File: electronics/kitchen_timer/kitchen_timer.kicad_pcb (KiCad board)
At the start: 2 copper layers, 76.5 x 84.5 mm, 30 parts, among them J1 JST_2pin_2.5mm, J2 UART, J3 SWD, Q1 BC327, Q2 BC327, Q3 BC327, Q4 BC327, Q5 BC337, SW1 BTN_A, SW2 BTN_B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

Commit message: Add 3d models to components, small rerouting
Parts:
- added H1: M2 hole, MountingHole:MountingHole_2.2mm_M2_Pad_Via, F.Cu at (74.0, 91.8)
- added H2: M2 hole, MountingHole:MountingHole_2.2mm_M2_Pad_Via, F.Cu at (139.0, 91.8)
- added H3: M2 hole, MountingHole:MountingHole_2.2mm_M2_Pad_Via, F.Cu at (139.0, 20.8)
- added H4: M2 hole, MountingHole:MountingHole_2.2mm_M2_Pad_Via, F.Cu at (74.0, 20.8)
- J1: moved to B.Cu
- moved J1 39.6 mm to (122.2, 55.5), turned to 0 degrees
- moved J2 9.91 mm to (124.2, 92.0), turned to -90 degrees
- moved SW1 4.15 mm to (134.8, 31.5)
- moved SW2 4.15 mm to (134.8, 51.5)
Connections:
- U2 pad 23: unconnected-(U2-GND-Pad23) -> GND
- U2 pad 28: unconnected-(U2-GND-Pad28) -> GND
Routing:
- net Net-(U2-GPIO4): track 112.4 -> 79.7 mm
- net /charging_and_audio/VSYS: track 29.2 -> 18.8 mm
- net Net-(U2-GPIO8): track 63.7 -> 55.7 mm
- net Net-(J2-Pin_2): track 10.8 -> 4.16 mm
- net Net-(U2-GPIO10): track 81.9 -> 75.9 mm
- net Net-(U2-GPIO12): track 68.8 -> 62.8 mm
- net Net-(U2-GPIO14): track 89.4 -> 85.4 mm
- net Net-(U2-GPIO5): track 71.1 -> 67.3 mm
- net Net-(U2-GPIO11): track 75.8 -> 73.3 mm
- net Net-(Q1-B): track 6.19 -> 7.92 mm
- net Net-(J2-Pin_3): track 5.33 -> 4.16 mm
- net Net-(U2-GPIO13): track 68.2 -> 67.0 mm
- net Net-(U2-GPIO15): track 73.6 -> 72.5 mm
- net /charging_and_audio/PWM_SPEAKER: track 14.0 -> 13.0 mm
- net IN_2: track 31.9 -> 31.3 mm
- added copper zone on B.Cu, net GND
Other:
- board size 76.5 x 84.5 mm -> 74.2 x 79 mm

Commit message: Update electronics
- added Schottky diode and solder bridge
- corrected all errors from design rules checker
- added silk screen logos
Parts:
- added D1: SEMTECH BAT54S, Package_TO_SOT_SMD:TSOT-23, B.Cu at (119.0, 56.2)
- added G***: LOGO, LOGO, F.Cu at (104.2, 78.8)
- added G***: LOGO, LOGO, F.Cu at (127.8, 23.8)
- added JP1: SCHOTTKY_JUMPER, Jumper:SolderJumper-2_P1.3mm_Open_Pad1.0x1.5mm, B.Cu at (118.8, 51.5)
- added TP1: PWM_SPEAKER, TestPoint:TestPoint_Pad_2.0x2.0mm, F.Cu at (105.5, 66.8)
- U2: value Pico -> Raspberry Pi Pico
- moved J1 3.50 mm to (125.8, 55.5), turned to 90 degrees
- moved R14 1.77 mm to (132.2, 58.8)
- moved Q5 1.03 mm to (127.2, 62.8)
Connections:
- net /charging_and_audio/PWM_SPEAKER renamed /PWM_SPEAKER
- J1 pad 1: /charging_and_audio/VSYS -> /charging_and_audio/OUT+
- U2 pad 13: unconnected-(U2-GND-Pad13) -> GND
- U2 pad 18: unconnected-(U2-GND-Pad18) -> GND
- U2 pad 8: unconnected-(U2-GND-Pad8) -> GND
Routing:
- net /charging_and_audio/OUT+: track 0.00 -> 10.2 mm
- net /charging_and_audio/VSYS: track 18.8 -> 24.4 mm
- net Net-(Q1-E): track 104.1 -> 107.8 mm
- net /PWM_SPEAKER: track 13.0 -> 16.3 mm
- net VCC: track 40.1 -> 37.1 mm
- net Net-(Q5-C): track 30.5 -> 27.7 mm
- net Net-(U2-GPIO7): track 70.1 -> 72.5 mm
- net Net-(Q5-B): track 8.83 -> 7.64 mm
- net Net-(U2-GPIO5): track 67.3 -> 66.5 mm
- net Net-(Q3-C): track 8.27 -> 7.59 mm
- net Net-(U1-G): track 9.63 -> 9.01 mm
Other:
- board text added: "Kryštof Hes v1.0 2024"
- board text added: "Raspberry Pi Pico"
- board text added: "TimeUp Kitchen Timer"

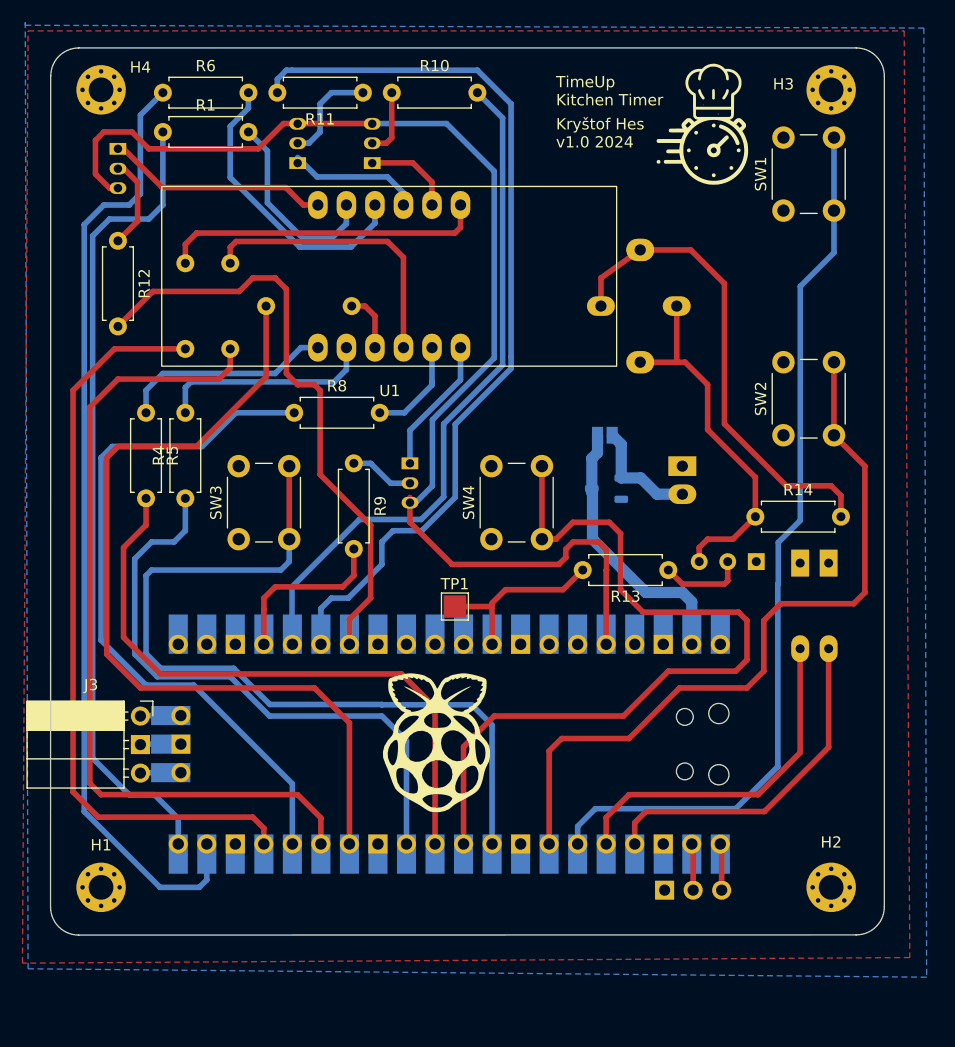
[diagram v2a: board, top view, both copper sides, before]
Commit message: Update electronics
- resistors with longer spacing between holes
- GND for SWD
- solder jumper new footprint
- increase distances between nets

- added datasheet for schottky
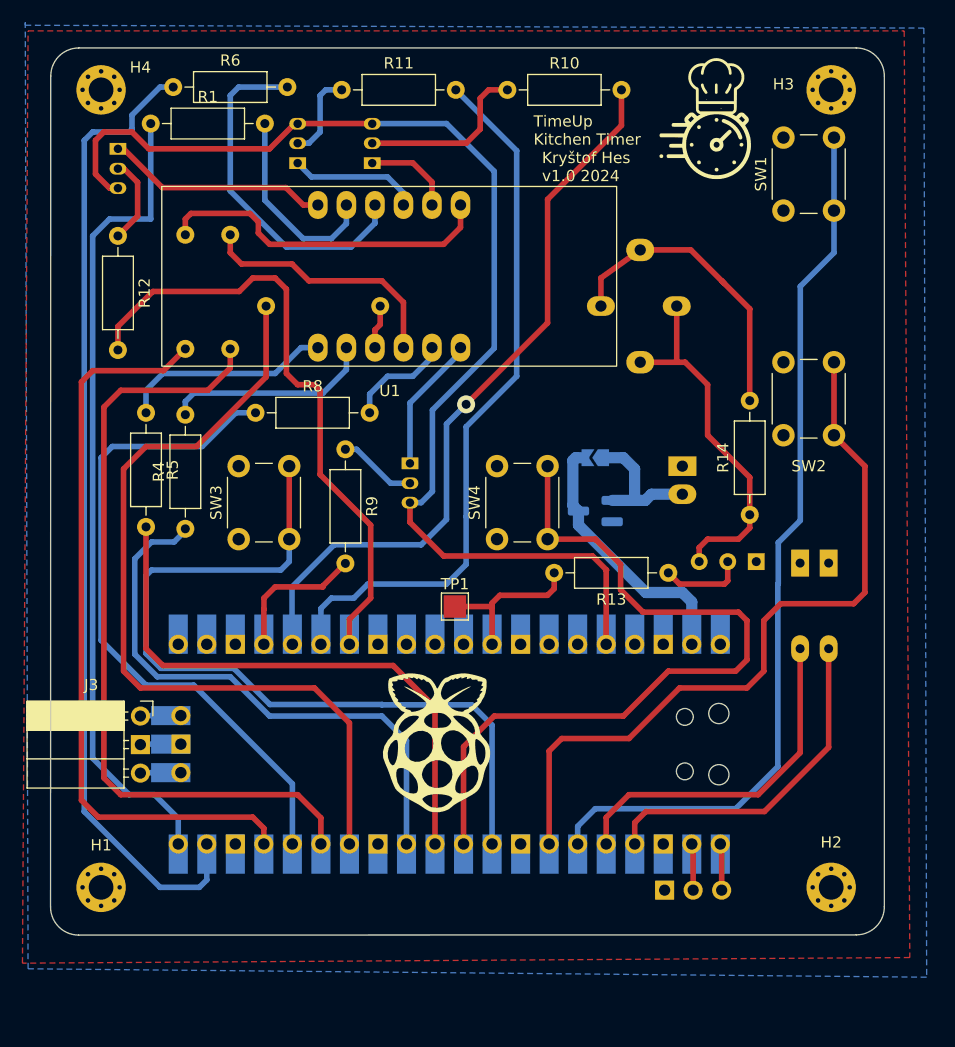
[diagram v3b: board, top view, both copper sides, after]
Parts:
- D1: footprint Package_TO_SOT_SMD:TSOT-23 -> Custom_footprints:SOT-23_Handsoldering_renumbered
- JP1: footprint Jumper:SolderJumper-2_P1.3mm_Open_Pad1.0x1.5mm -> Jumper:SolderJumper-2_P1.3mm_Open_TrianglePad1.0x1.5mm
- R1, R10, R11, R12, R13, R14, R2, R3, R4, R5, R6, R7, R8, R9: footprint Resistor_THT:R_Axial_DIN0207_L6.3mm_D2.5mm_P7.62mm_Horizontal -> Resistor_THT:R_Axial_DIN0207_L6.3mm_D2.5mm_P10.16mm_Horizontal
- U2: value Raspberry Pi Pico -> Pico
- moved R10 10.3 mm to (110.2, 20.8)
- moved R8 3.44 mm to (87.8, 49.5)
- moved R4 2.71 mm to (81.5, 59.8)
- moved D1 2.24 mm to (118.0, 58.2)
- moved JP1 2.17 mm to (118.0, 53.5)
- moved R11 1.91 mm to (95.4, 20.8), turned to 0 degrees
- moved R9 1.46 mm to (95.8, 52.8)
- moved R1 1.31 mm to (78.4, 23.8)
- moved R6 1.05 mm to (80.4, 20.5)
- moved G*** 0.56 mm to (128.0, 23.2)
- moved R14 0.53 mm to (131.8, 58.6), turned to 90 degrees
- moved SW4 0.50 mm to (109.2, 60.8)
- moved R12 0.44 mm to (75.5, 33.8)
- moved R13 0.25 mm to (124.5, 63.8)
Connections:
- D1 pad 2: (no net) -> /charging_and_audio/VSYS
- D1 pad 3: /charging_and_audio/VSYS -> (no net)
- J3 pad 2: Net-(J3-Pin_2) -> GND
- U2 pad 42: Net-(J3-Pin_2) -> GND
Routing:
- net Net-(U2-GPIO20): track 81.7 -> 64.1 mm
- net VCC: track 37.1 -> 21.4 mm
- net Net-(Q3-B): track 5.95 -> 15.6 mm
- net Net-(U1-F): track 26.2 -> 31.3 mm
- net Net-(U2-GPIO19): track 61.0 -> 66.1 mm, vias 0 -> 1
- net Net-(U2-GPIO8): track 55.7 -> 50.9 mm
- net Net-(J3-Pin_2): track 3.67 -> 0.00 mm
- net GND: track 0.00 -> 3.67 mm
- net Net-(U2-GPIO12): track 62.8 -> 59.3 mm
- net Net-(U2-GPIO7): track 72.5 -> 69.2 mm
- net Net-(Q1-E): track 107.8 -> 104.5 mm
- net Net-(U2-GPIO9): track 53.5 -> 50.6 mm
- net Net-(U1-C): track 25.7 -> 22.9 mm
- net Net-(U2-GPIO11): track 73.3 -> 70.5 mm
- net Net-(U2-GPIO10): track 75.9 -> 73.2 mm
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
